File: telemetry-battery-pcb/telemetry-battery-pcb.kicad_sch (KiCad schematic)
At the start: 67 parts, among them J1 Network Connector, J3 CONN_360410_MZC, J5 CONN_360410_MZC, Q1 NMOS, Q2 PMOS, Q4 NMOS, U4 LTC2944, U5 XR76208, U6 M24C02-WMN, U7 TPS1HTC30-Q1

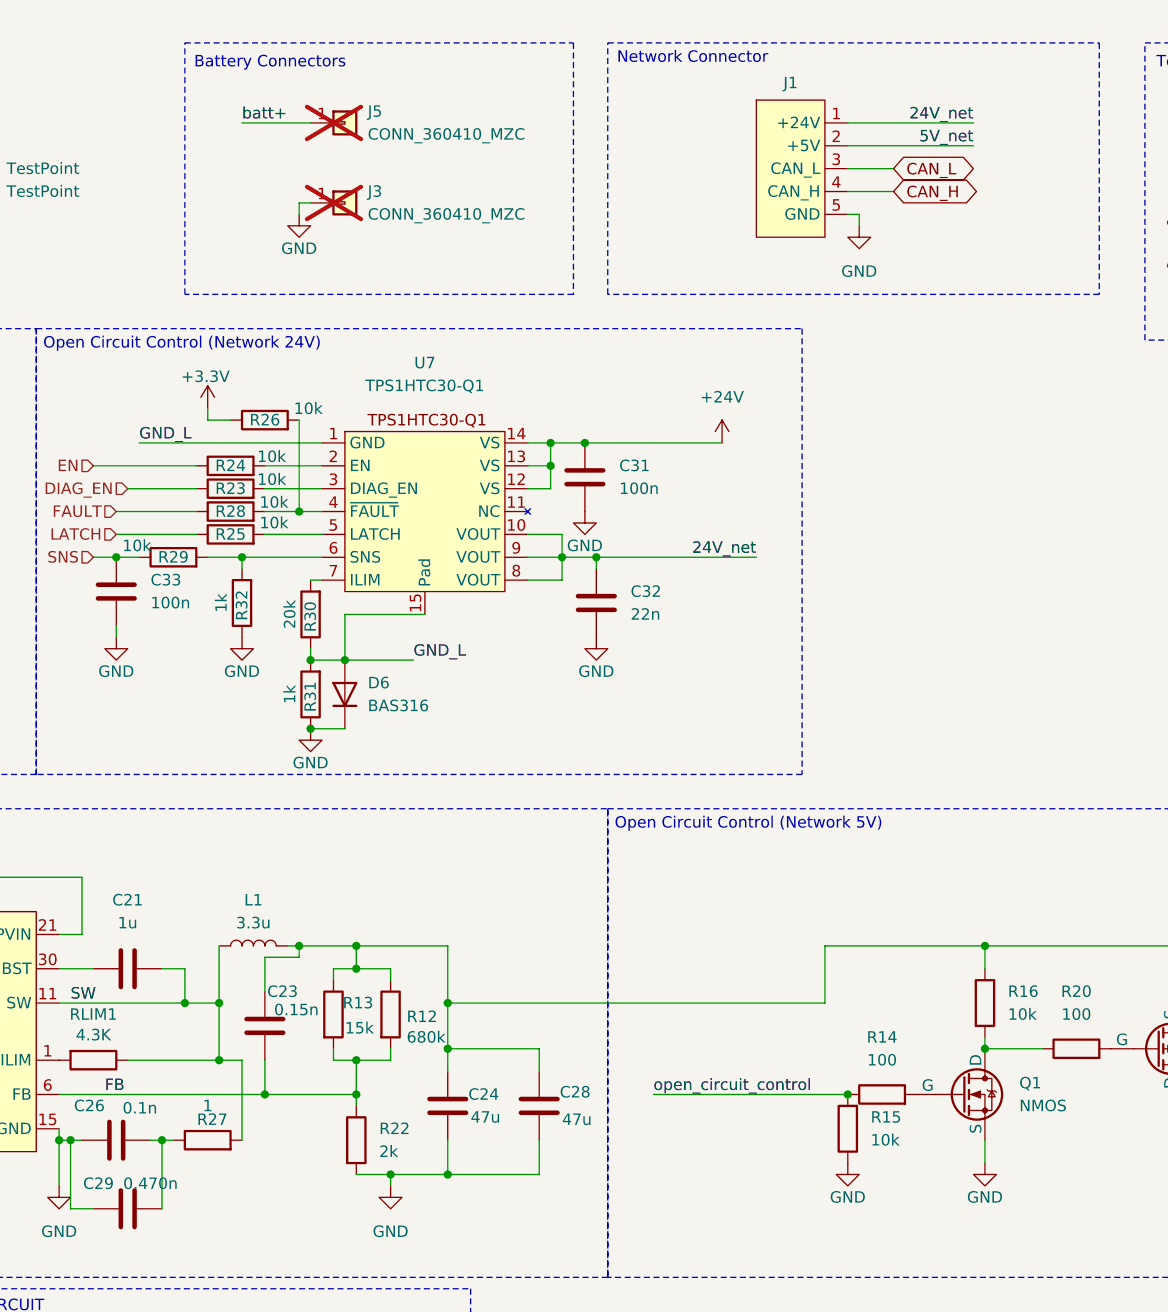
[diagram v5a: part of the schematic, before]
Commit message: telemetry-battery: modify footprint P-channel-Mosfet
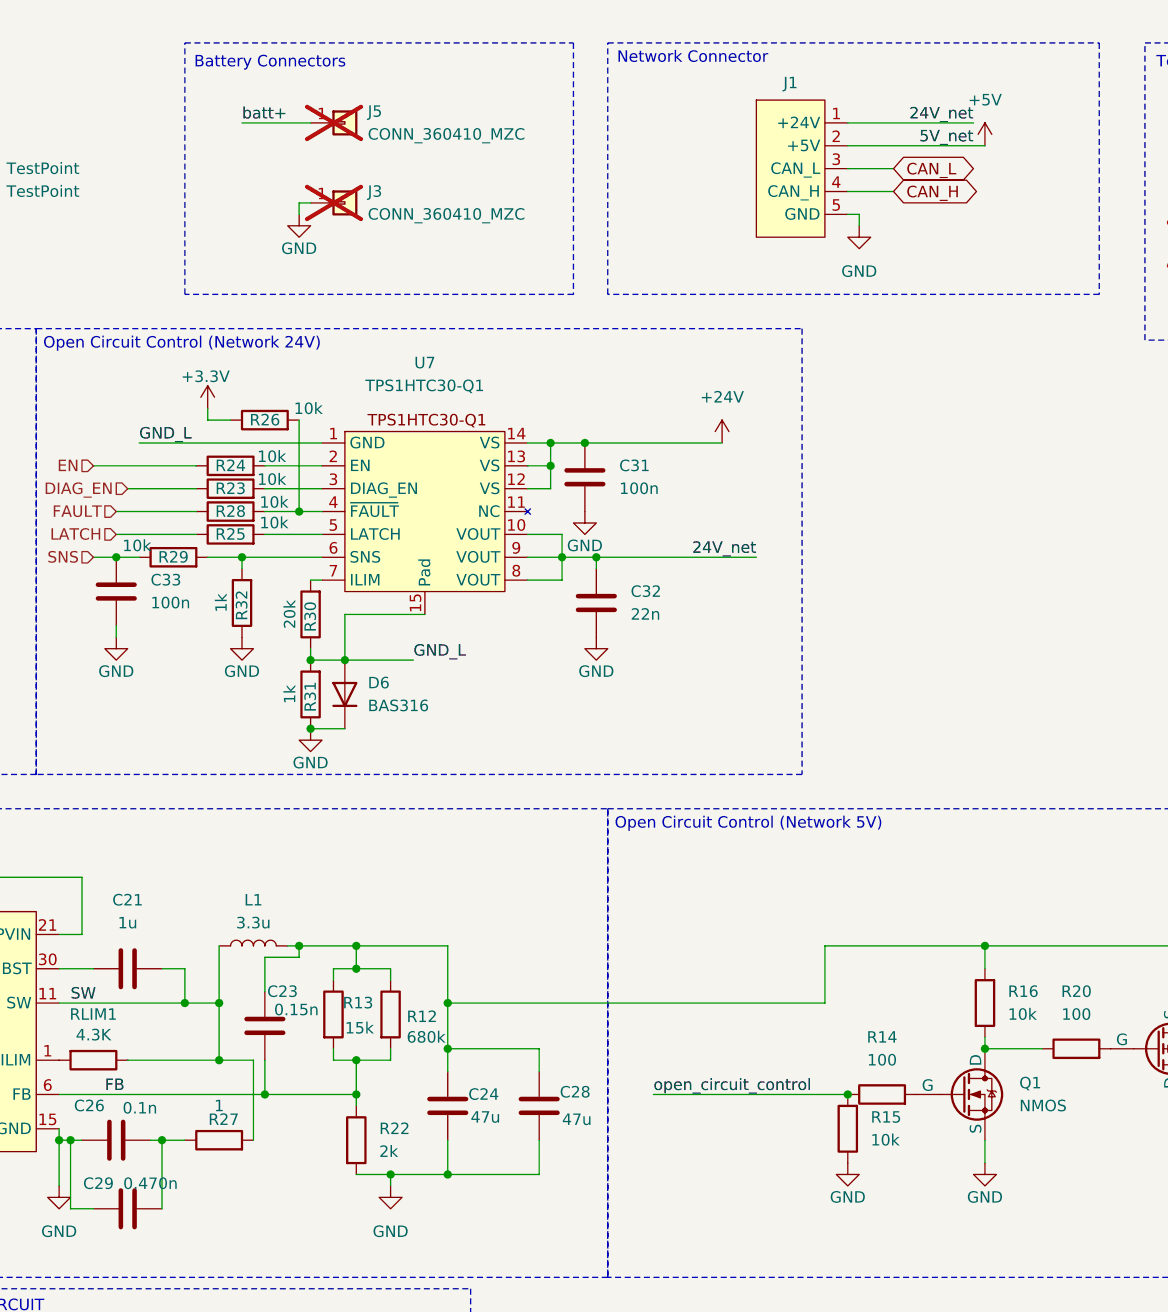
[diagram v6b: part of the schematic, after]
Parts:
- L1: footprint Inductor_SMD:L_0402_1005Metric -> Inductor_SMD:L_Sunlord_MWSA1005S
- Q2: footprint Package_SO:SO-8_3.9x4.9mm_P1.27mm -> Exocet:exocet_SO-8_3.9x4.9mm_P1.27mm_copy
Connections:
- net 5V_net renamed +5V
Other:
- moved on the sheet: R27
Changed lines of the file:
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@@
 	(wire
 		(pts
-			(xy 119.38 128.27) (xy 119.38 137.16)
+			(xy 120.65 128.27) (xy 120.65 137.16)
 		)
 		(stroke
@@
 	(wire
 		(pts
-			(xy 111.76 137.16) (xy 110.49 137.16)
+			(xy 113.03 137.16) (xy 110.49 137.16)
 		)
 		(stroke
@@
 	(wire
 		(pts
-			(xy 186.69 26.67) (xy 200.66 26.67)
+			(xy 186.69 26.67) (xy 201.93 26.67)
 		)
 		(stroke
@@
 	(wire
 		(pts
-			(xy 116.84 128.27) (xy 119.38 128.27)
+			(xy 116.84 128.27) (xy 120.65 128.27)
 		)
 		(stroke
@@
 			)
 		)
-		(property "Footprint" "Inductor_SMD:L_0402_1005Metric"
+		(property "Footprint" "Inductor_SMD:L_Sunlord_MWSA1005S"
 			(at 120.65 115.57 0)
 			(effects
@@
 			)
 		)
-		(property "Footprint" "Package_SO:SO-8_3.9x4.9mm_P1.27mm"
+		(property "Footprint" "Exocet:exocet_SO-8_3.9x4.9mm_P1.27mm_copy"
 			(at 226.06 129.54 0)
 			(effects
@@
 	(symbol
 		(lib_id "Device:R")
-		(at 115.57 137.16 90)
+		(at 116.84 137.16 90)
 		(unit 1)
 		(exclude_from_sim no)
@@
 		(dnp no)
 		(property "Reference" "R27"
-			(at 116.078 134.874 90)
+			(at 117.348 134.874 90)
 			(effects
 				(font
@@
 		)
 		(property "Value" "1"
-			(at 115.57 133.35 90)
+			(at 116.84 133.35 90)
 			(effects
 				(font
@@
 		)
 		(property "Footprint" "Resistor_SMD:R_0402_1005Metric"
-			(at 115.57 138.938 90)
+			(at 116.84 138.938 90)
 			(effects
 				(font
@@
 		)
 		(property "Datasheet" "~"
-			(at 115.57 137.16 0)
+			(at 116.84 137.16 0)
 			(effects
 				(font
@@
 		)
 		(property "Description" "Resistor"
-			(at 115.57 137.16 0)
+			(at 116.84 137.16 0)
 			(effects
 				(font
@@
 		)
 		(property "JLCPCB" "C25086"
-			(at 115.57 137.16 90)
+			(at 116.84 137.16 90)
 			(effects
 				(font
@@
 					(unit 1)
 				)
+			)
+		)
+	)
+	(symbol
+		(lib_id "power:+5V")
+		(at 201.93 26.67 0)
+		(unit 1)
+		(exclude_from_sim no)
+		(in_bom yes)
+		(on_board yes)
+		(dnp no)
+		(fields_autoplaced yes)
+		(property "Reference" "#PWR064"
+			(at 201.93 30.48 0)
+			(effects
+				(font
+					(size 1.27 1.27)
+				)
+				(hide yes)
+			)
+		)
+		(property "Value" "+5V"
+			(at 201.93 21.59 0)
+			(effects
+				(font
+					(size 1.27 1.27)
+				)
+			)
+		)
+		(property "Footprint" ""
+			(at 201.93 26.67 0)
+			(effects
+				(font
+					(size 1.27 1.27)
+				)
+				(hide yes)
+			)
+		)
+		(property "Datasheet" ""
+			(at 201.93 26.67 0)
+			(effects
+				(font
+					(size 1.27 1.27)
+				)
+				(hide yes)
+			)
+		)
+		(property "Description" "Power symbol creates a global label with name \"+5V\""
+			(at 201.93 26.67 0)
+			(effects
+				(font
+					(size 1.27 1.27)
+				)
+				(hide yes)
+			)
+		)
+		(pin "1"
+		)
+		(instances
+			(project ""
+				(path "/4b4cf3aa-c94c-4150-b9c5-35049cd71136"
+					(reference "#PWR064")
+					(unit 1)
+				)

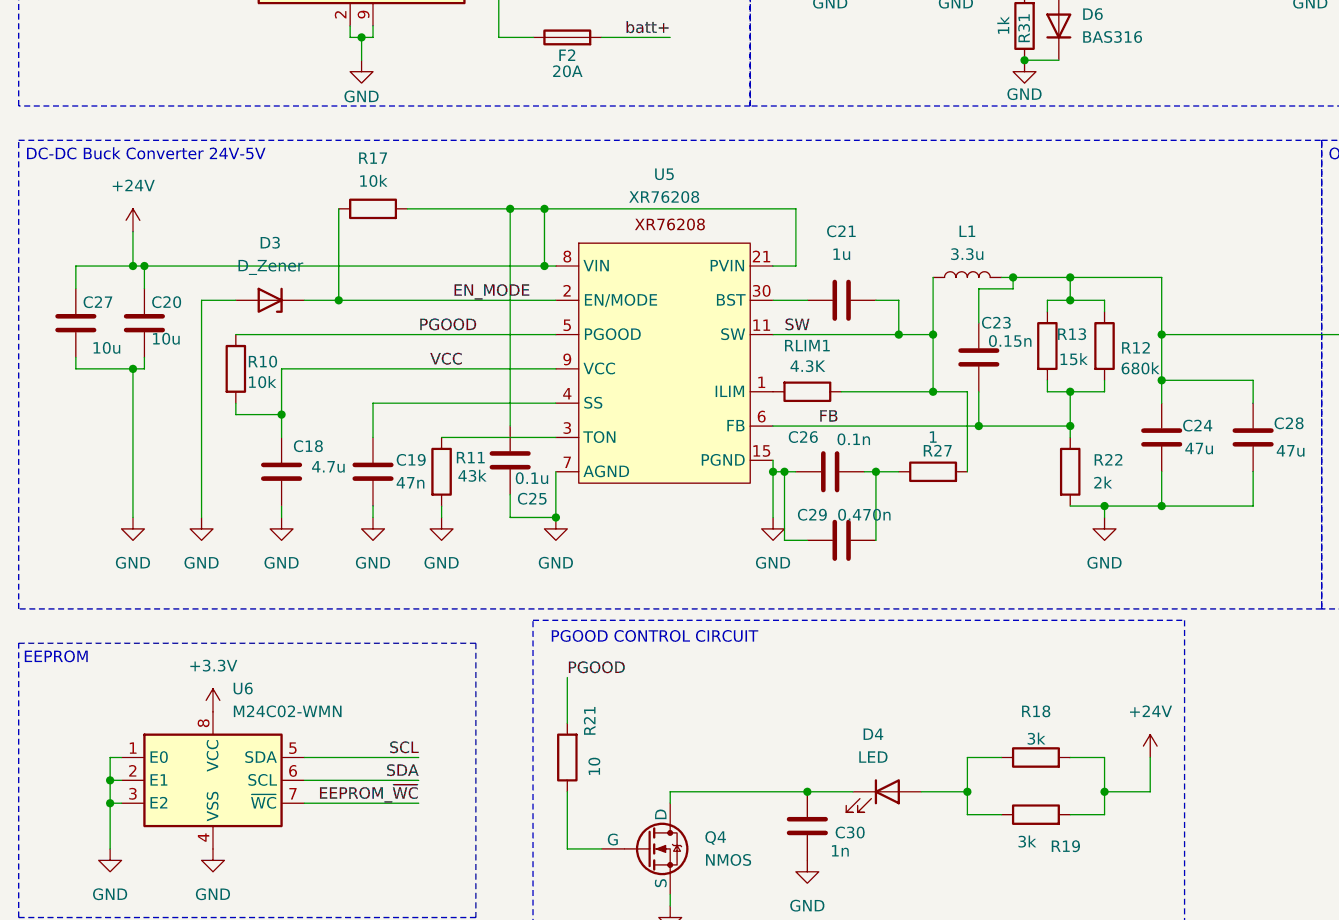
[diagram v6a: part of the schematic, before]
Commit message: telemetry-battery : Routing of PCB
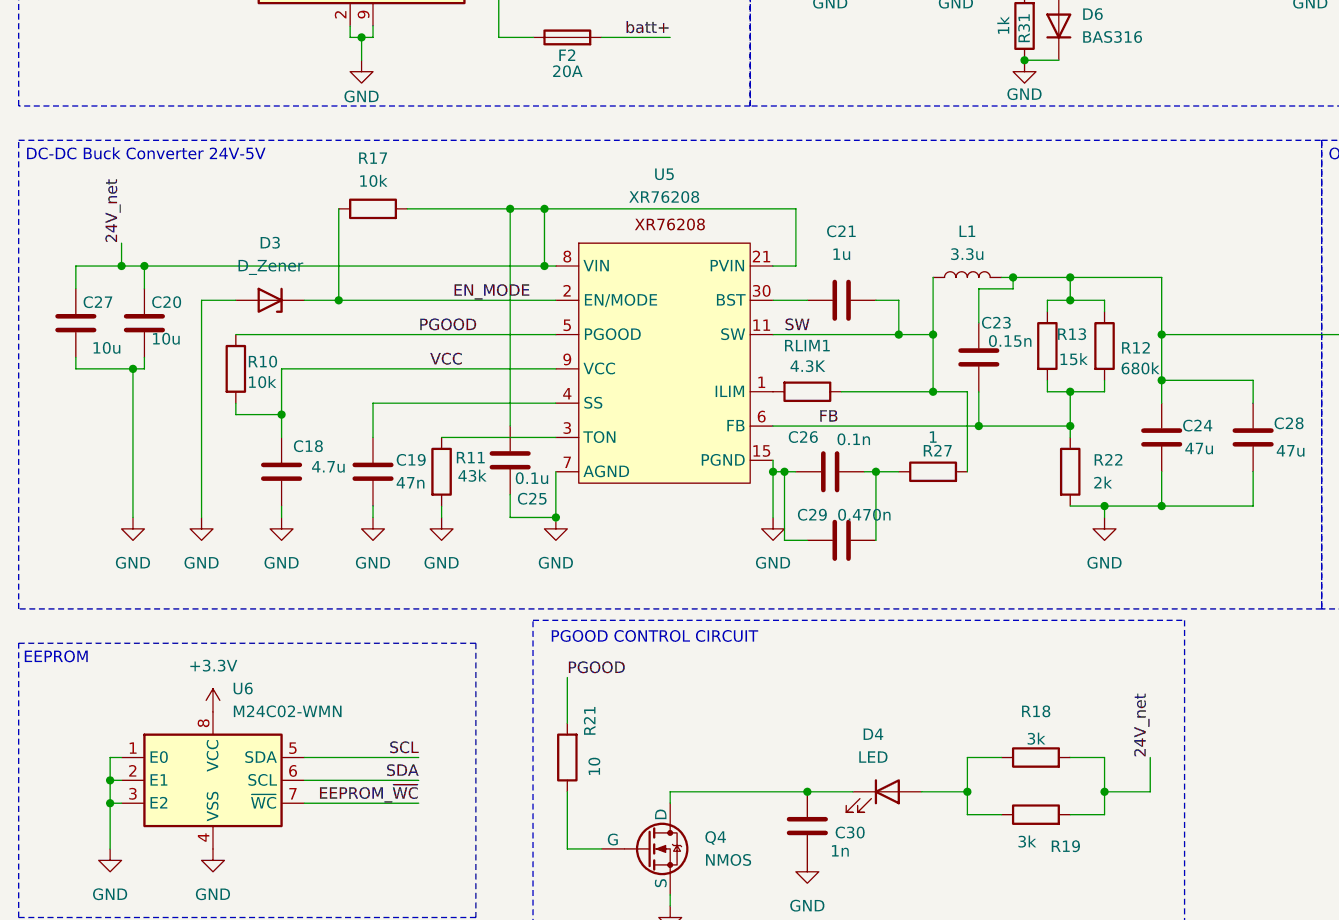
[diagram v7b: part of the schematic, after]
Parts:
- U7: footprint Exocet:Tps1htc30_Texas_HTSSOP-14-1EP_4.4x5mm_P0.65mm_EP3.4x5mm_Mask3.155x3.255mm_ThermalVias -> Package_SO:Texas_HTSSOP-14-1EP_4.4x5mm_P0.65mm_EP3.4x5mm_Mask3.155x3.255mm_ThermalVias
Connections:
- net +24V: no longer C20.1, C25.1, C27.1, R17.2, R18.2, R19.2, U5.21 (PVIN), U5.8 (VIN)
- net 24V_net: now also C20.1, C25.1, C27.1, R17.2, R18.2, R19.2, U5.21 (PVIN), U5.8 (VIN)
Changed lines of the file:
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@@
 	)
 	(junction
+		(at 26.67 114.3)
+		(diameter 0)
+		(color 0 0 0 0)
+	)
+	(junction
 		(at 116.84 121.92)
 		(diameter 0)
@@
 	)
 	(junction
-		(at 27.94 114.3)
-		(diameter 0)
-		(color 0 0 0 0)
-	)
-	(junction
 		(at 102.87 172.72)
 		(diameter 0)
@@
 	(wire
 		(pts
-			(xy 29.21 114.3) (xy 27.94 114.3)
-		)
-		(stroke
-			(width 0)
-			(type default)
-		)
-	)
-	(wire
-		(pts
 			(xy 116.84 121.92) (xy 116.84 128.27)
 		)
@@
 	(wire
 		(pts
+			(xy 26.67 114.3) (xy 29.21 114.3)
+		)
+		(stroke
+			(width 0)
+			(type default)
+		)
+	)
+	(wire
+		(pts
 			(xy 118.11 57.15) (xy 115.57 57.15)
 		)
@@
 	(wire
 		(pts
-			(xy 21.59 114.3) (xy 27.94 114.3)
+			(xy 21.59 114.3) (xy 26.67 114.3)
 		)
 		(stroke
@@
 	(wire
 		(pts
-			(xy 27.94 110.49) (xy 27.94 114.3)
+			(xy 26.67 111.76) (xy 26.67 114.3)
 		)
 		(stroke
@@
 		)
 	)
+	(label "24V_net"
+		(at 140.97 168.91 90)
+		(effects
+			(font
+				(size 1.27 1.27)
+			)
+			(justify left bottom)
+		)
+	)
 	(label "PGOOD"
 		(at 59.69 121.92 0)
@@
 		)
 	)
+	(label "24V_net"
+		(at 26.67 111.76 90)
+		(effects
+			(font
+				(size 1.27 1.27)
+			)
+			(justify left bottom)
+		)
+	)
 	(label "EEPROM_~{WC}"
 		(at 59.69 173.99 180)
@@
 	)
 	(symbol
-		(lib_id "power:+24V")
-		(at 27.94 110.49 0)
-		(unit 1)
-		(exclude_from_sim no)
-		(in_bom yes)
-		(on_board yes)
-		(dnp no)
-		(fields_autoplaced yes)
-		(property "Reference" "#PWR050"
-			(at 27.94 114.3 0)
-			(effects
-				(font
-					(size 1.27 1.27)
-				)
-				(hide yes)
-			)
-		)
-		(property "Value" "+24V"
-			(at 27.94 105.41 0)
-			(effects
-				(font
-					(size 1.27 1.27)
-				)
-			)
-		)
-		(property "Footprint" ""
-			(at 27.94 110.49 0)
-			(effects
-				(font
-					(size 1.27 1.27)
-				)
-				(hide yes)
-			)
-		)
-		(property "Datasheet" ""
-			(at 27.94 110.49 0)
-			(effects
-				(font
-					(size 1.27 1.27)
-				)
-				(hide yes)
-			)
-		)
-		(property "Description" "Power symbol creates a global label with name \"+24V\""
-			(at 27.94 110.49 0)
-			(effects
-				(font
-					(size 1.27 1.27)
-				)
-				(hide yes)
-			)
-		)
-		(pin "1"
-		)
-		(instances
-			(project ""
-				(path "/4b4cf3aa-c94c-4150-b9c5-35049cd71136"
-					(reference "#PWR050")
-					(unit 1)
-				)
-			)
-		)
-	)
-	(symbol
 		(lib_id "Device:R")
 		(at 62.23 137.16 0)
@@
 	)
 	(symbol
-		(lib_id "power:+24V")
-		(at 140.97 168.91 0)
-		(unit 1)
-		(exclude_from_sim no)
-		(in_bom yes)
-		(on_board yes)
-		(dnp no)
-		(fields_autoplaced yes)
-		(property "Reference" "#PWR052"
-			(at 140.97 172.72 0)
-			(effects
-				(font
-					(size 1.27 1.27)
-				)
-				(hide yes)
-			)
-		)
-		(property "Value" "+24V"
-			(at 140.97 163.83 0)
-			(effects
-				(font
-					(size 1.27 1.27)
-				)
-			)
-		)
-		(property "Footprint" ""
-			(at 140.97 168.91 0)
-			(effects
-				(font
-					(size 1.27 1.27)
-				)
-				(hide yes)
-			)
-		)
-		(property "Datasheet" ""
-			(at 140.97 168.91 0)
-			(effects
-				(font
-					(size 1.27 1.27)
-				)
-				(hide yes)
-			)
-		)
-		(property "Description" "Power symbol creates a global label with name \"+24V\""
-			(at 140.97 168.91 0)
-			(effects
-				(font
-					(size 1.27 1.27)
-				)
-				(hide yes)
-			)
-		)
-		(pin "1"
-		)
-		(instances
-			(project "telemetry-battery-pcb"
-				(path "/4b4cf3aa-c94c-4150-b9c5-35049cd71136"
-					(reference "#PWR052")
-					(unit 1)
-				)
-			)
-		)
-	)
-	(symbol
 		(lib_id "Device:C")
 		(at 152.4 133.35 0)
@@
 			)
 		)
-		(property "Footprint" "Exocet:Tps1htc30_Texas_HTSSOP-14-1EP_4.4x5mm_P0.65mm_EP3.4x5mm_Mask3.155x3.255mm_ThermalVias"
+		(property "Footprint" "Package_SO:Texas_HTSSOP-14-1EP_4.4x5mm_P0.65mm_EP3.4x5mm_Mask3.155x3.255mm_ThermalVias"
 			(at 139.7 53.34 0)
 			(effects
